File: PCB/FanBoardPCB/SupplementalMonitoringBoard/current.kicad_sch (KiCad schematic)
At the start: 8 parts, among them U2 OPA842xDBV

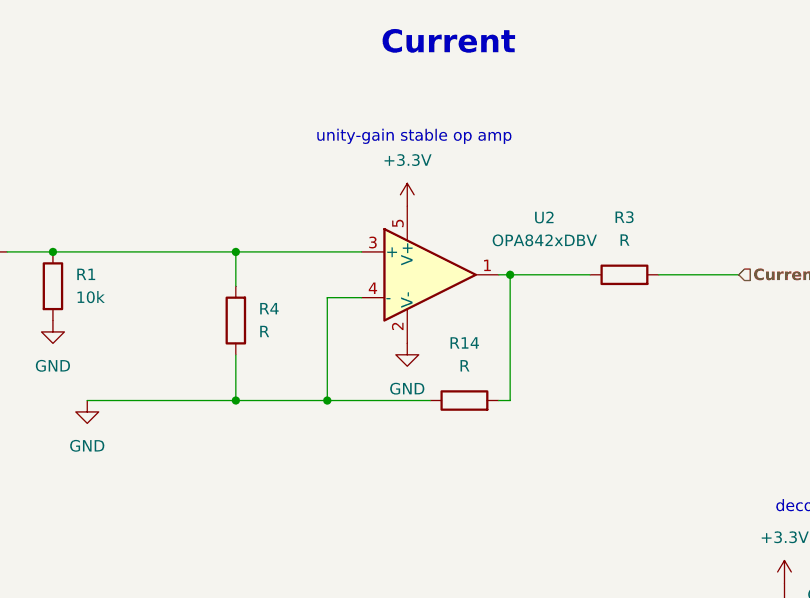
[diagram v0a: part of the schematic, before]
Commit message: Supplemental Monitoring Board
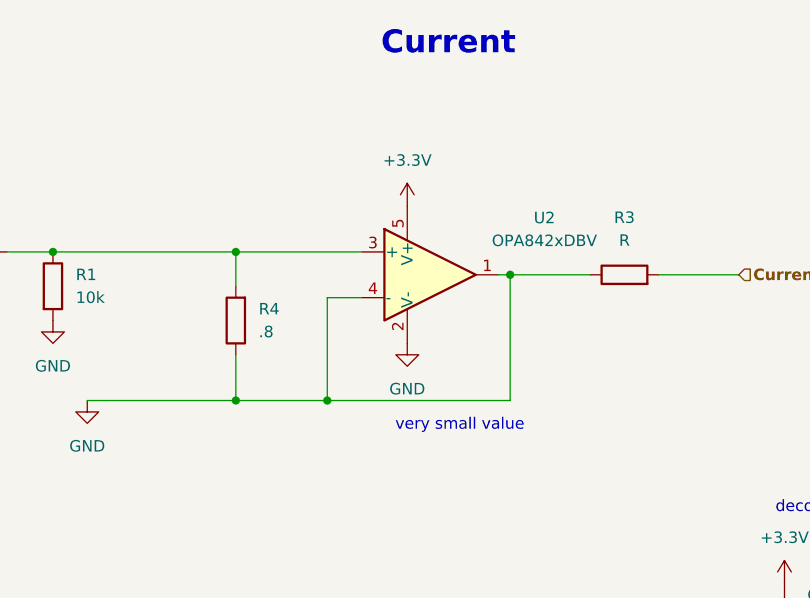
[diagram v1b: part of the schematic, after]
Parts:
- removed R14: R, symbol Device:R
- R4: value R -> .8
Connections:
- net GND: now also R3.1, U2.1
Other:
- note added: "very small value"
- note removed: "unity-gain stable op amp"
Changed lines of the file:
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@@
 	(wire
 		(pts
-			(xy 129.54 106.68) (xy 140.97 106.68)
+			(xy 129.54 106.68) (xy 149.86 106.68)
 		)
 		(stroke
@@
 		(pts
 			(xy 129.54 95.25) (xy 133.35 95.25)
-		)
-		(stroke
-			(width 0)
-			(type default)
-		)
-	)
-	(wire
-		(pts
-			(xy 148.59 106.68) (xy 149.86 106.68)
 		)
 		(stroke
@@
 		)
 	)
-	(text "unity-gain stable op amp"
-		(exclude_from_sim no)
-		(at 139.192 77.47 0)
-		(effects
-			(font
-				(size 1.27 1.27)
-				(thickness 0.1588)
-			)
-		)
-	)
 	(text "decoupling capacitor"
 		(exclude_from_sim no)
@@
 				(size 1.27 1.27)
 				(thickness 0.1588)
+			)
+		)
+	)
+	(text "very small value\n"
+		(exclude_from_sim no)
+		(at 144.272 109.474 0)
+		(effects
+			(font
+				(size 1.27 1.27)
 			)
 		)
@@
 			)
 		)
-		(property "Value" "R"
+		(property "Value" ".8"
 			(at 121.92 99.0599 0)
 			(effects
@@
 					(unit 1)
 				)
-			)
-		)
-	)
-	(symbol
-		(lib_id "Device:R")
-		(at 144.78 106.68 90)
-		(unit 1)
-		(exclude_from_sim no)
-		(in_bom yes)
-		(on_board yes)
-		(dnp no)
-		(fields_autoplaced yes)
-		(property "Reference" "R14"
-			(at 144.78 100.33 90)
-			(effects
-				(font
-					(size 1.27 1.27)
-				)
-			)
-		)
-		(property "Value" "R"
-			(at 144.78 102.87 90)
-			(effects
-				(font
-					(size 1.27 1.27)
-				)
-			)
-		)
-		(property "Footprint" ""
-			(at 144.78 108.458 90)
-			(effects
-				(font
-					(size 1.27 1.27)
-				)
-				(hide yes)
-			)
-		)
-		(property "Datasheet" "~"
-			(at 144.78 106.68 0)
-			(effects
-				(font
-					(size 1.27 1.27)
-				)
-				(hide yes)
-			)
-		)
-		(property "Description" "Resistor"
-			(at 144.78 106.68 0)
-			(effects
-				(font
-					(size 1.27 1.27)
-				)
-				(hide yes)
-			)
-		)
-		(pin "1"
-		)
-		(pin "2"
-		)
-		(instances
-			(project "SupplementalMonitoringBoard"
-				(path "/aa0415d0-3287-4bc4-9a8e-766ada9ace2f/1e74c2bc-637a-422a-831e-fab1291cbb0a"
-					(reference "R14")
-					(unit 1)
-				)
